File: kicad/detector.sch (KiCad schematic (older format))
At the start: 45 parts, among them J1 Conn_01x05_Male, J2 Conn_01x05_Male, U1 LT1761-5, U2 LT1964-5, U3 REF5010ID, U4 OPA2197xD, U5 OPA2197xD

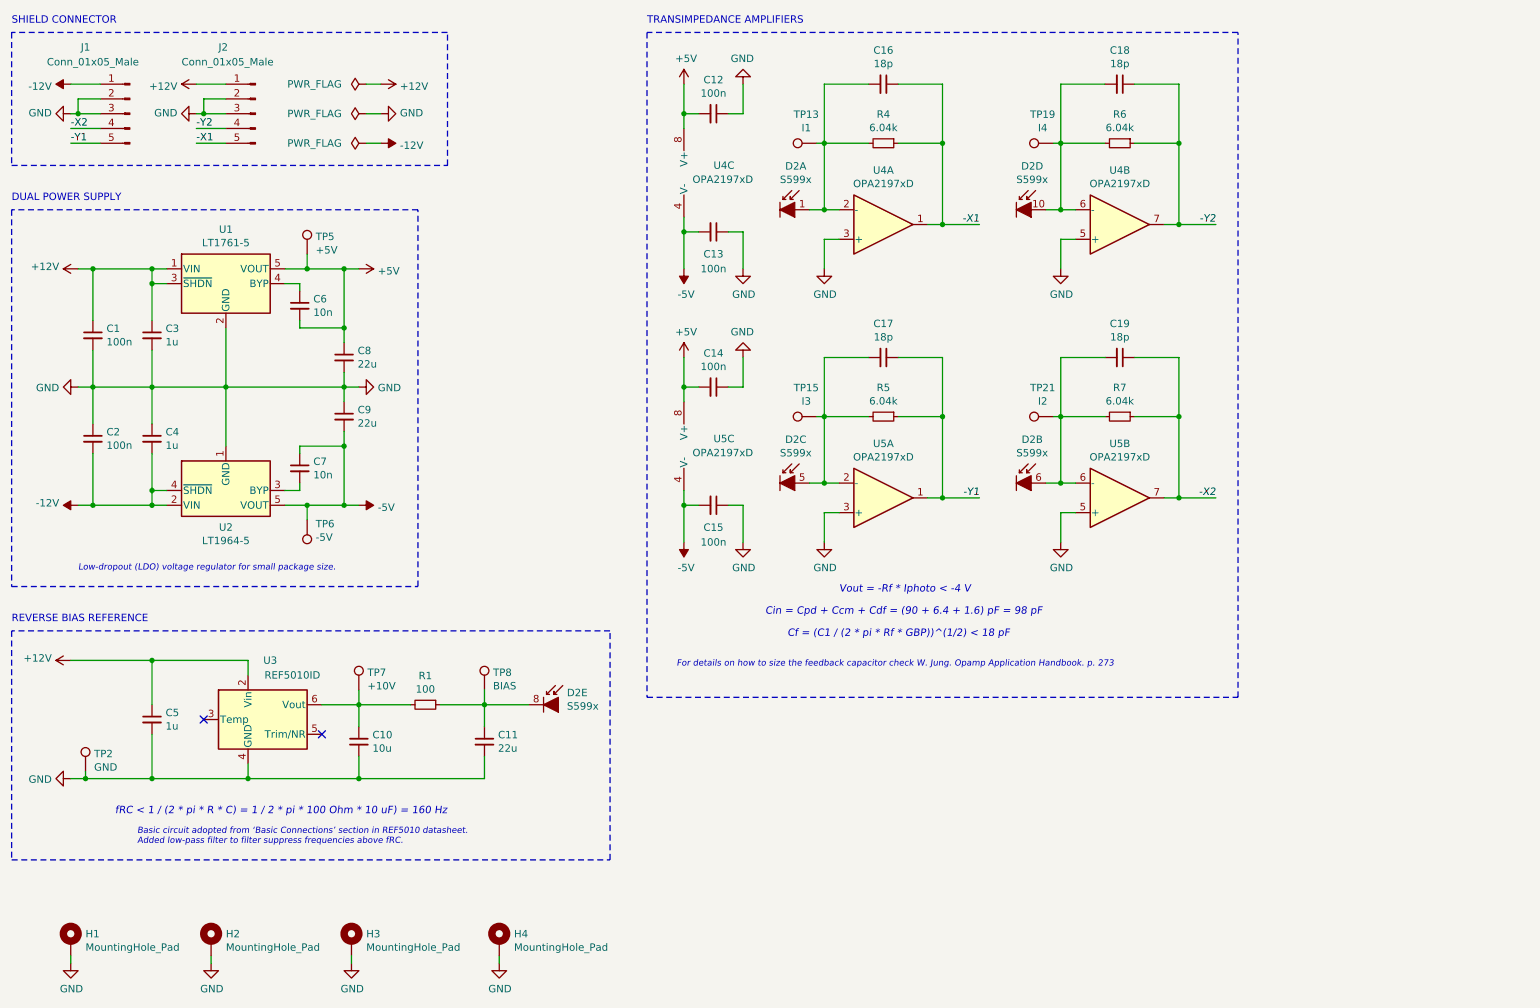
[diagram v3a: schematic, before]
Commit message: redesigned detector pcb
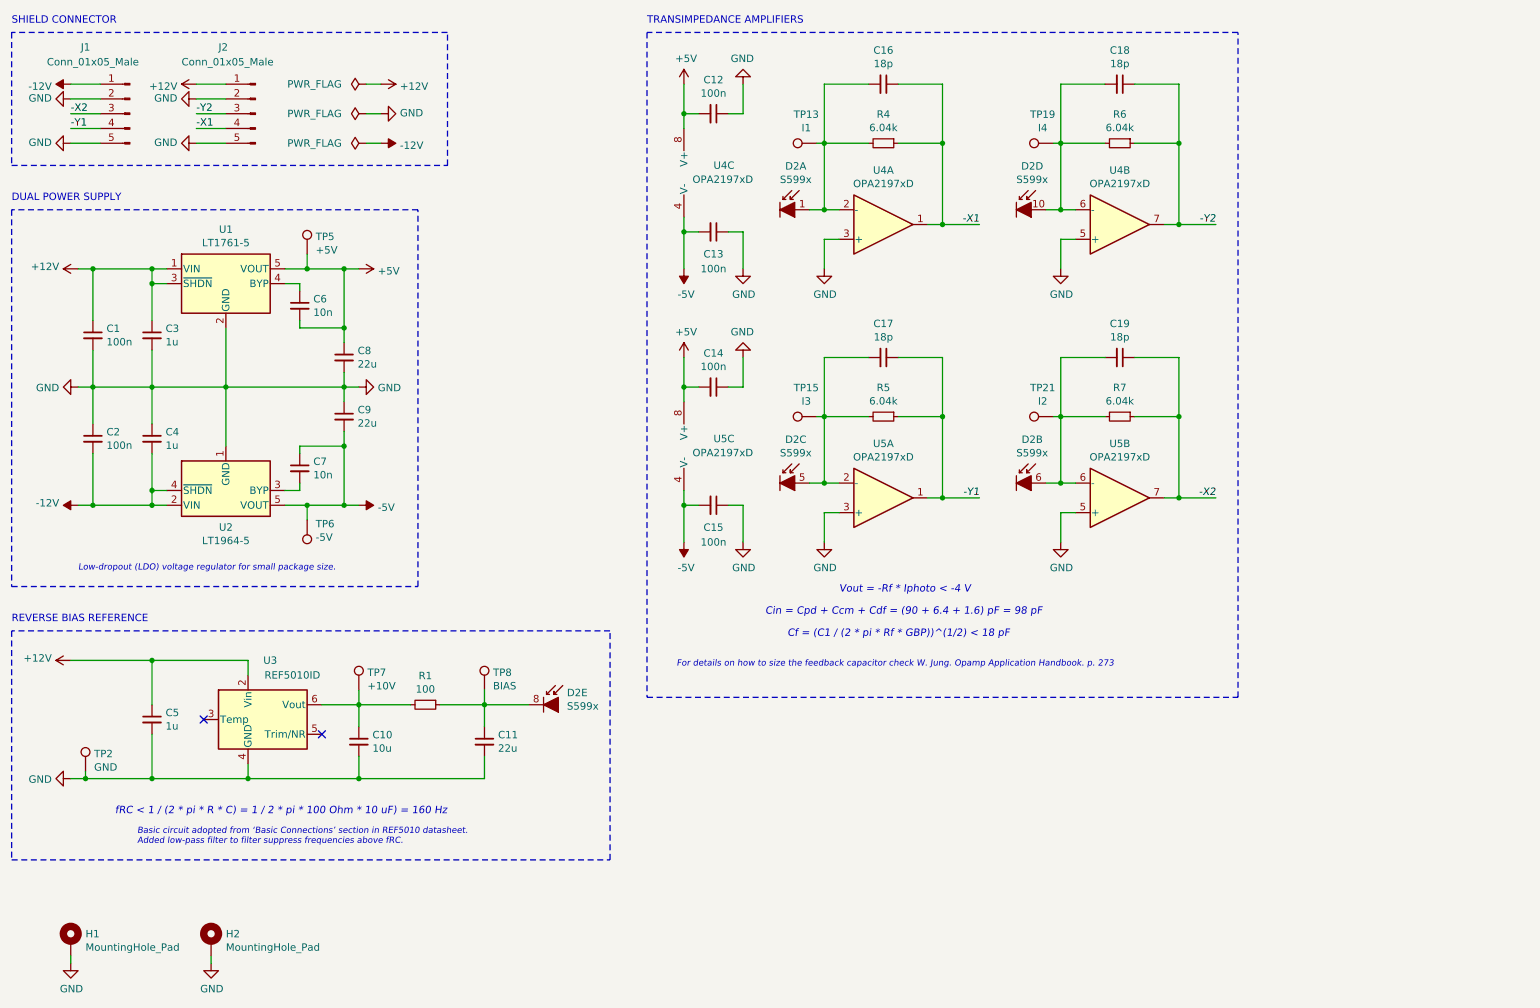
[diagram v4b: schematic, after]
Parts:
- removed H3, H4: MountingHole_Pad, MountingHole:MountingHole_2.7mm_M2.5_Pad, symbol Mechanical:MountingHole_Pad
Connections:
- net -X1: now also J2.4 (Pin_4); no longer J2.5 (Pin_5)
- net -X2: now also J1.3 (Pin_3); no longer J1.4 (Pin_4)
- net -Y1: now also J1.4 (Pin_4); no longer J1.5 (Pin_5)
- net -Y2: now also J2.3 (Pin_3); no longer J2.4 (Pin_4)
- net GND: now also J1.5 (Pin_5), J2.5 (Pin_5); no longer J1.3 (Pin_3), J2.3 (Pin_3)
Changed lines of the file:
@@
 	1    0    0    1
 $EndComp
-Text Label 2000 1550 0    50   ~ 0
+Text Label 2000 1450 0    50   ~ 0
 -X1
-Text Label 1150 1450 0    50   ~ 0
+Text Label 1150 1350 0    50   ~ 0
 -X2
 Wire Wire Line
-	2050 1250 2200 1250
-Wire Wire Line
-	2050 1350 2200 1350
+	2000 1250 2200 1250
 Wire Wire Line
 	2000 1450 2200 1450
@@
 	3150 1550 3250 1550
 Wire Wire Line
-	1200 1350 1150 1350
-Wire Wire Line
 	1350 1150 1150 1150
 Wire Wire Line
 	1350 1550 1150 1550
-Wire Wire Line
-	1200 1250 1350 1250
-Wire Wire Line
-	1200 1350 1200 1250
-Connection ~ 1200 1350
 $Comp
 L power:-12V #PWR0110
@@
 L power:GND #PWR0111
 U 1 1 5E9D8FA6
-P 1150 1350
-F 0 "#PWR0111" H 1150 1100 50  0001 C CNN
-F 1 "GND" V 1155 1222 50  0000 R CNN
-F 2 "" H 1150 1350 50  0001 C CNN
-F 3 "" H 1150 1350 50  0001 C CNN
-	1    1150 1350
+P 1150 1250
+F 0 "#PWR0111" H 1150 1000 50  0001 C CNN
+F 1 "GND" V 1155 1122 50  0000 R CNN
+F 2 "" H 1150 1250 50  0001 C CNN
+F 3 "" H 1150 1250 50  0001 C CNN
+	1    1150 1250
 	0    1    -1   0
 $EndComp
-Wire Wire Line
-	1350 1350 1200 1350
 $Comp
 L Connector:Conn_01x05_Male J1
@@
 Wire Wire Line
 	1300 4000 1700 4000
-Text Label 2000 1450 0    50   ~ 0
+Text Label 2000 1350 0    50   ~ 0
 -Y2
-Text Label 1150 1550 0    50   ~ 0
+Text Label 1150 1450 0    50   ~ 0
 -Y1
 $Comp
@@
 $EndComp
 $Comp
-L Mechanical:MountingHole_Pad H3
-U 1 1 5EA3BD34
-P 3050 6950
-F 0 "H3" H 3150 6999 50  0000 L CNN
-F 1 "MountingHole_Pad" H 3150 6908 50  0000 L CNN
-F 2 "MountingHole:MountingHole_2.7mm_M2.5_Pad" H 3050 6950 50  0001 C CNN
-F 3 "~" H 3050 6950 50  0001 C CNN
-	1    3050 6950
-	1    0    0    -1
-$EndComp
-$Comp
-L Mechanical:MountingHole_Pad H4
-U 1 1 5EA3BF9A
-P 4050 6950
-F 0 "H4" H 4150 6999 50  0000 L CNN
-F 1 "MountingHole_Pad" H 4150 6908 50  0000 L CNN
-F 2 "MountingHole:MountingHole_2.7mm_M2.5_Pad" H 4050 6950 50  0001 C CNN
-F 3 "~" H 4050 6950 50  0001 C CNN
-	1    4050 6950
-	1    0    0    -1
-$EndComp
-$Comp
 L power:GND #PWR0115
 U 1 1 5EA3CCB1
@@
 Wire Wire Line
 	2100 7100 2100 7050
-$Comp
-L power:GND #PWR0117
-U 1 1 5EA50D8F
-P 3050 7100
-F 0 "#PWR0117" H 3050 6850 50  0001 C CNN
-F 1 "GND" H 3055 6927 50  0000 C CNN
-F 2 "" H 3050 7100 50  0001 C CNN
-F 3 "" H 3050 7100 50  0001 C CNN
-	1    3050 7100
-	1    0    0    -1
-$EndComp
-Wire Wire Line
-	3050 7100 3050 7050
-$Comp
-L power:GND #PWR0118
-U 1 1 5EA64F10
-P 4050 7100
-F 0 "#PWR0118" H 4050 6850 50  0001 C CNN
-F 1 "GND" H 4055 6927 50  0000 C CNN
-F 2 "" H 4050 7100 50  0001 C CNN
-F 3 "" H 4050 7100 50  0001 C CNN
-	1    4050 7100
-	1    0    0    -1
-$EndComp
-Wire Wire Line
-	4050 7100 4050 7050
-Wire Wire Line
-	2050 1350 2050 1250
-Connection ~ 2050 1350
 Wire Wire Line
 	1150 1450 1350 1450
@@
 	0    -1   1    0
 $EndComp
-Wire Wire Line
-	2050 1350 2000 1350
 $Comp
 L power:GND #PWR0112
 U 1 1 5ED37047
-P 2000 1350
-F 0 "#PWR0112" H 2000 1100 50  0001 C CNN
-F 1 "GND" V 2005 1222 50  0000 R CNN
-F 2 "" H 2000 1350 50  0001 C CNN
-F 3 "" H 2000 1350 50  0001 C CNN
-	1    2000 1350
+P 2000 1250
+F 0 "#PWR0112" H 2000 1000 50  0001 C CNN
+F 1 "GND" V 2005 1122 50  0000 R CNN
+F 2 "" H 2000 1250 50  0001 C CNN
+F 3 "" H 2000 1250 50  0001 C CNN
+	1    2000 1250
 	0    1    -1   0
 $EndComp
@@
 Text Notes 750  750  0    50   ~ 0
 SHIELD CONNECTOR
+Wire Wire Line
+	1150 1350 1350 1350
+Wire Wire Line
+	1150 1250 1350 1250
+$Comp
+L power:GND #PWR0117
+U 1 1 5EA5A8AA
+P 1150 1550
+F 0 "#PWR0117" H 1150 1300 50  0001 C CNN
+F 1 "GND" V 1155 1422 50  0000 R CNN
+F 2 "" H 1150 1550 50  0001 C CNN
+F 3 "" H 1150 1550 50  0001 C CNN
+	1    1150 1550
+	0    1    -1   0
+$EndComp
+Wire Wire Line
+	2000 1350 2200 1350
+$Comp
+L power:GND #PWR0118
+U 1 1 5EA63D80
+P 2000 1550
+F 0 "#PWR0118" H 2000 1300 50  0001 C CNN
+F 1 "GND" V 2005 1422 50  0000 R CNN
+F 2 "" H 2000 1550 50  0001 C CNN
+F 3 "" H 2000 1550 50  0001 C CNN
+	1    2000 1550
+	0    1    -1   0
+$EndComp
 $EndSCHEMATC

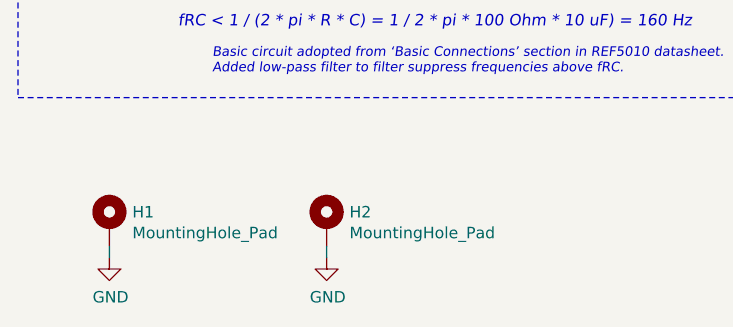
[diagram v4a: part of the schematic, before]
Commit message: fix some DRC errors, remove some test points
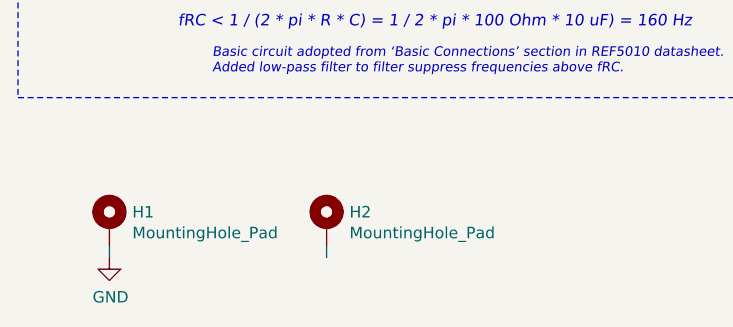
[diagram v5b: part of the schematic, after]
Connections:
- net GND: no longer H2.1
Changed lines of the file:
@@
 Wire Wire Line
 	1150 7100 1150 7050
-$Comp
-L power:GND #PWR0116
-U 1 1 5EA46D11
-P 2100 7100
-F 0 "#PWR0116" H 2100 6850 50  0001 C CNN
-F 1 "GND" H 2105 6927 50  0000 C CNN
-F 2 "" H 2100 7100 50  0001 C CNN
-F 3 "" H 2100 7100 50  0001 C CNN
-	1    2100 7100
-	1    0    0    -1
-$EndComp
 Wire Wire Line
 	2100 7100 2100 7050
